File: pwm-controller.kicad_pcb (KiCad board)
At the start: 4 copper layers, 50 x 50 mm, 57 parts, among them J1 DEBUG_ADDRESS_I2C_INT, J4 POWER, J5 OUT+, J6 OUT-, Q1 MMBT5551, Q10 MMBT5551, Q2 MMBT5401, Q3 NTMS4807, Q4 NTMS4807, Q5 MMBT5551, Q6 MMBT5401, Q7 NTMS4807, Q8 NTMS4807, Q9 MMBT5551, SW1 EC12D1524403, U1 STM8S003F3Px, U2 78L05

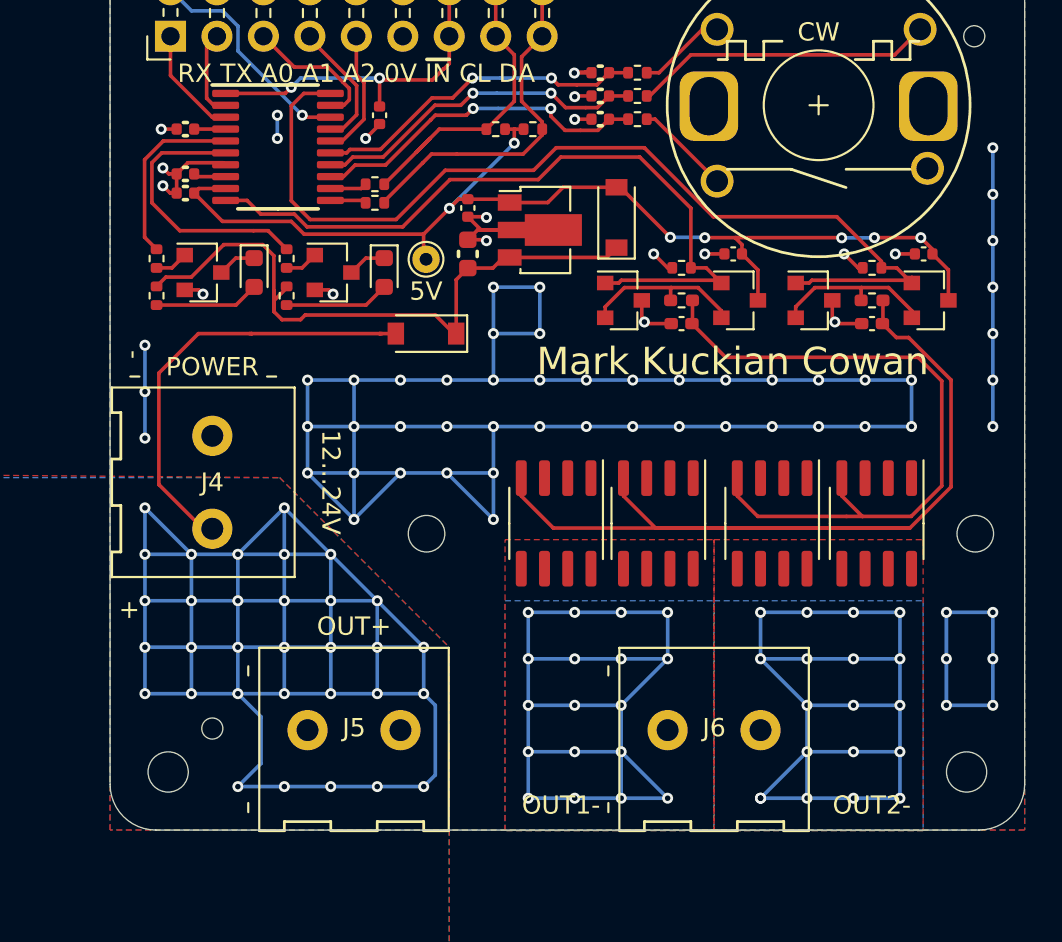
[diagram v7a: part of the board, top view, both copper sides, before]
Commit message: we can tolerate higher frequencies as long as our led strips are only a dozen or so metres long
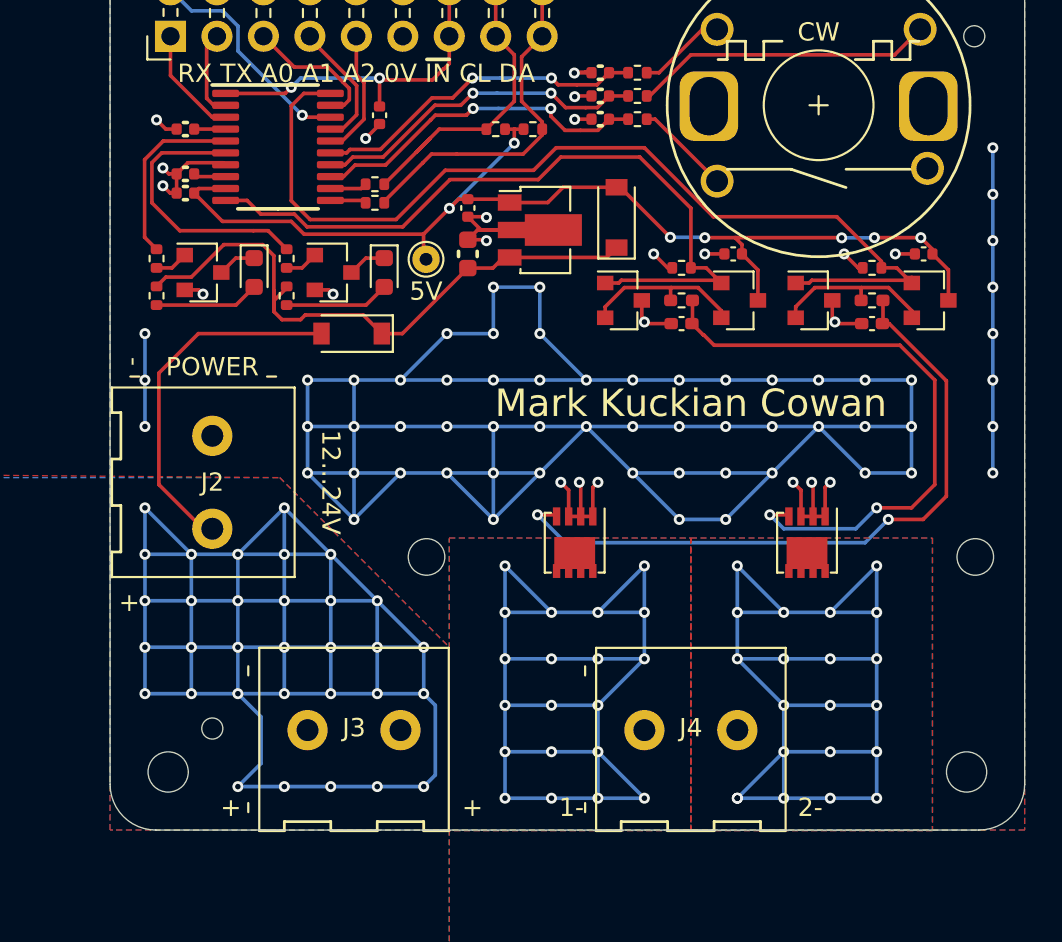
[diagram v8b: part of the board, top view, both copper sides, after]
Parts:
- removed the Q3 at (118.1, 109.4)
- removed the Q4 at (112.4, 109.4)
- removed the Q7 at (106.2, 109.4)
- removed the Q8 at (100.6, 109.4)
- added Q2: SiS402DN, Package_SO:Vishay_PowerPAK_1212-8_Single, F.Cu at (114.3, 110.5)
- added Q5: SiS402DN, Package_SO:Vishay_PowerPAK_1212-8_Single, F.Cu at (101.6, 110.5)
- C11, C13: value 3.3n -> 100n/50
- R10, R8: value 4.7k -> 220
- moved D2 4.06 mm to (89.4, 99.1)
- moved H3 1.27 mm to (93.5, 111.3)
- moved H6 1.27 mm to (123.5, 111.3)
- moved J4 1.27 mm to (108.0, 120.7)
- renumbered D4 to D1, D1 to D2, D2 to D3, D3 to D4, H8 to H7, J4 to J2, J5 to J3, J6 to J4, Q2 to Q3, Q5 to Q4, Q9 to Q7, Q10 to Q8
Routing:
- net GND: track 188.5 -> 237.1 mm, vias 74 -> 83
- net /channel2/GATE: track 59.2 -> 37.5 mm, vias 0 -> 2
- net DRAIN1: track 58.0 -> 70.2 mm, vias 19 -> 21
- net DRAIN2: track 58.0 -> 70.2 mm, vias 18 -> 20
- net /channel1/GATE: track 37.8 -> 33.0 mm, vias 0 -> 2
- net VIN: track 168.1 -> 163.8 mm
- net VIN_D: track 36.8 -> 35.1 mm
